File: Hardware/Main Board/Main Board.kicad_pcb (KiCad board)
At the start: 2 copper layers, 55 parts, among them J1 Micro_SD_Card_Det1, J2 Camera Module, J3 Conn_01x09_Socket, J4 MIC 1 Connector, J5 MIC 2 Connector, J6 USB_C_Receptacle_USB2.0_16P, J7 Conn_01x04_Socket, SW1 SW_Push, SW2 SW_Push, SW3 SW_Push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

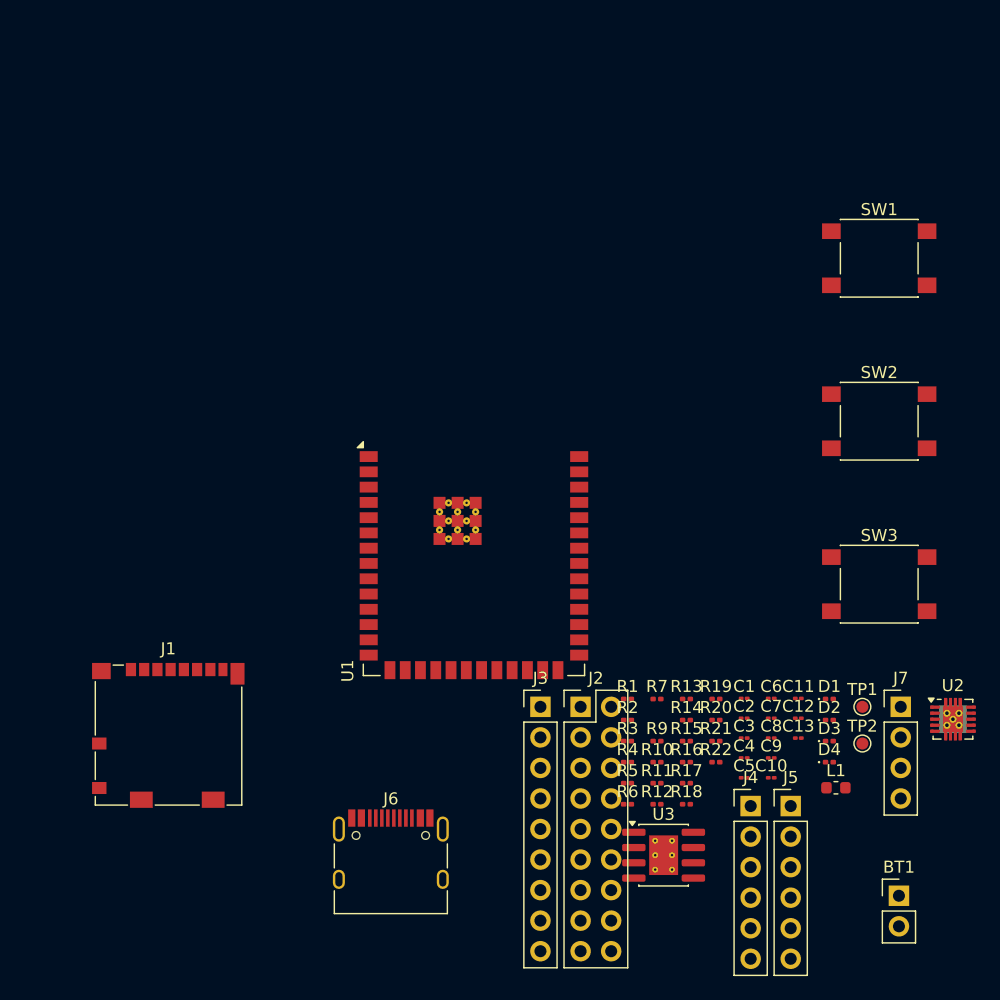
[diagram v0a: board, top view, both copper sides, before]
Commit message: drafted main board layout
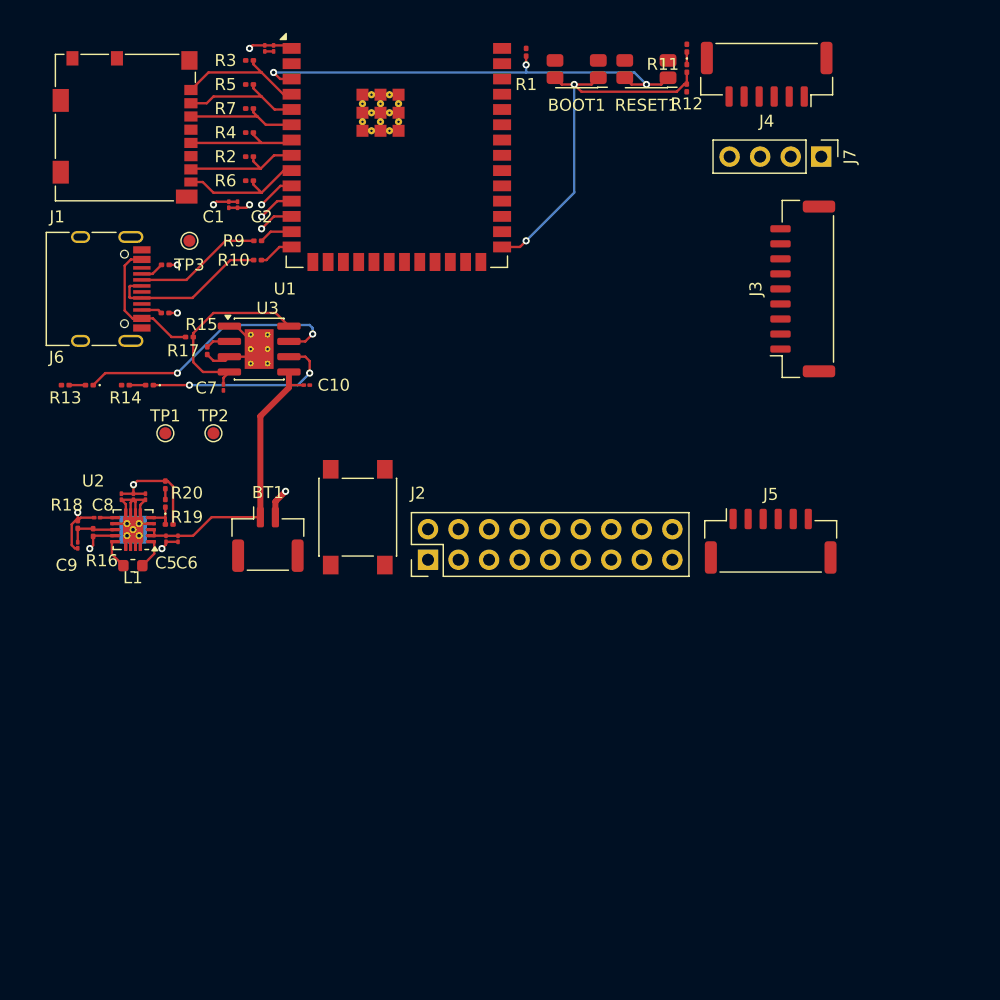
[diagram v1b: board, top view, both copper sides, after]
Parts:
- removed SW1, SW2, SW3: SW_Push, Button_Switch_SMD:SW_SPST_PTS645
- added BOOT1: SW_Push, Button_Switch_SMD:SW_SPST_EVQP7A, F.Cu at (119.2, 51.7)
- added RESET1: SW_Push, Button_Switch_SMD:SW_SPST_EVQP7A, F.Cu at (125.0, 51.7)
- added TP3: TestPoint, TestPoint:TestPoint_Pad_D1.0mm, F.Cu at (87.0, 66.0)
- added USER_INPUT1: SW_Push, Button_Switch_SMD:SW_SPST_PTS645, F.Cu at (101.0, 89.0)
- BT1: footprint Connector_PinHeader_2.54mm:PinHeader_1x02_P2.54mm_Vertical -> Connector_JST:JST_GH_SM02B-GHS-TB_1x02-1MP_P1.25mm_Horizontal
- J3: footprint Connector_PinHeader_2.54mm:PinHeader_1x09_P2.54mm_Vertical -> Connector_JST:JST_GH_SM09B-GHS-TB_1x09-1MP_P1.25mm_Horizontal
- J4, J5: footprint Connector_PinHeader_2.54mm:PinHeader_1x06_P2.54mm_Vertical -> Connector_JST:JST_GH_SM06B-GHS-TB_1x06-1MP_P1.25mm_Horizontal
- J7: value Conn_01x04_Socket -> OLED
- moved C4 70.8 mm to (94.0, 50.0), turned to 90 degrees
- moved U2 70.0 mm to (82.3, 90.0), turned to 180 degrees
- moved C3 69.8 mm to (93.3, 50.0), turned to -90 degrees
- moved D2 67.5 mm to (78.7, 78.0), turned to 180 degrees
- moved R5 66.1 mm to (92.0, 53.0), turned to 180 degrees
- moved R3 64.7 mm to (92.0, 51.0), turned to 180 degrees
- moved D3 63.8 mm to (83.7, 78.0), turned to 180 degrees
- moved TP1 62.3 mm to (85.0, 82.0)
- moved R22 61.7 mm to (85.0, 68.0)
- moved L1 61.3 mm to (82.3, 93.0)
- moved R4 61.1 mm to (92.0, 57.0)
- moved J4 60.9 mm to (135.0, 52.1), turned to 180 degrees
- moved R6 60.6 mm to (92.0, 61.0)
- moved C9 60.3 mm to (77.7, 91.3), turned to 90 degrees
- moved BT1 60.3 mm to (93.5, 90.8)
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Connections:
- J3 pad 7: I2C_SDA -> I2C_SCL
- J3 pad 8: I2C_SCL -> I2C_SDA
- J4 pad 2: MIC_LCRL -> GND
- J4 pad 3: MIC_DOUT -> MIC_BCLK
- J4 pad 4: MIC_BCLK -> MIC_DOUT
- J4 pad 5: MIC_GND -> MIC_LCRL
- J4 pad 6: MIC_3V -> +3.3V
- J5 pad 1: GND -> +3.3V
- J5 pad 2: MIC_LCRL -> GND
- J5 pad 3: MIC_DOUT -> MIC_BCLK
- J5 pad 4: MIC_BCLK -> MIC_DOUT
- J5 pad 5: MIC_GND -> MIC_LCRL
- J5 pad 6: MIC_3V -> GND
- U1 pad 10: CAM_D7 -> CAM_CLK
- U1 pad 11: CAM_PCLK -> CAM_SIO_DAT
- U1 pad 12: CAM_D0 -> CAM_HREF
- U1 pad 15: CAM_XCLK -> CAM_VSYNC
- U1 pad 16: CAM_HREF -> CAM_XCLK
- U1 pad 17: CAM_D1 -> CAM_PCLK
- U1 pad 18: CAM_D2 -> CAM_D6
- U1 pad 19: CAM_D3 -> CAM_D7
- U1 pad 22: CAM_D6 -> CAM_D2
- U1 pad 23: CAM_VSYNC -> CAM_D3
- U1 pad 24: CAM_SIO_DAT -> CAM_D0
- U1 pad 25: CAM_CLK -> CAM_D1
- U1 pad 26: CONTACT_MCLK -> Net-(U1-IO45)
- U1 pad 32: MIC_LCRL -> MIC_DOUT
- U1 pad 33: MIC_DOUT -> MIC_LCRL
- U1 pad 34: I2C_SDA -> CONTACT_SCLK
- U1 pad 35: I2C_SCL -> CONTACT_LRCK
- U1 pad 37: CONTACT_SCLK -> CONTACT_MCLK
- U1 pad 38: CONTACT_LRCK -> I2C_SCL
- U1 pad 39: Net-(U1-IO1) -> I2C_SDA
- U1 pad 4: SD_CLK -> SD_D2
- U1 pad 5: SD_CMD -> SD_D3
- U1 pad 6: SD_D0 -> SD_CMD
- U1 pad 7: SD_D1 -> SD_CLK
- U1 pad 8: SD_D2 -> SD_D0
- U1 pad 9: SD_D3 -> SD_D1
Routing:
- net Net-(U1-EN): track 0.00 -> 38.6 mm, vias 0 -> 3
- net GND: track 0.00 -> 34.2 mm, vias 0 -> 7
- net Net-(U1-IO0): track 0.00 -> 31.8 mm, vias 0 -> 2
- net +BATT: track 0.00 -> 24.3 mm
- net Net-(D2-K): track 0.00 -> 23.2 mm, vias 0 -> 2
- net Net-(D3-K): track 0.00 -> 16.3 mm, vias 0 -> 2
- net Net-(U3-CE): track 0.00 -> 16.1 mm
- net +3.3V: track 0.00 -> 15.1 mm, vias 0 -> 3
- net USB_D+: track 0.00 -> 13.6 mm
- net +5V_USB: track 0.00 -> 11.5 mm
- net SD_D2: track 0.00 -> 11.0 mm
- net SD_D1: track 0.00 -> 10.8 mm
- net USB_D-: track 0.00 -> 10.7 mm
- net SD_D3: track 0.00 -> 10.3 mm
- net SD_D0: track 0.00 -> 10.1 mm
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
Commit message: revised main board layout, rearranged around strapping pins, rererouted for noise
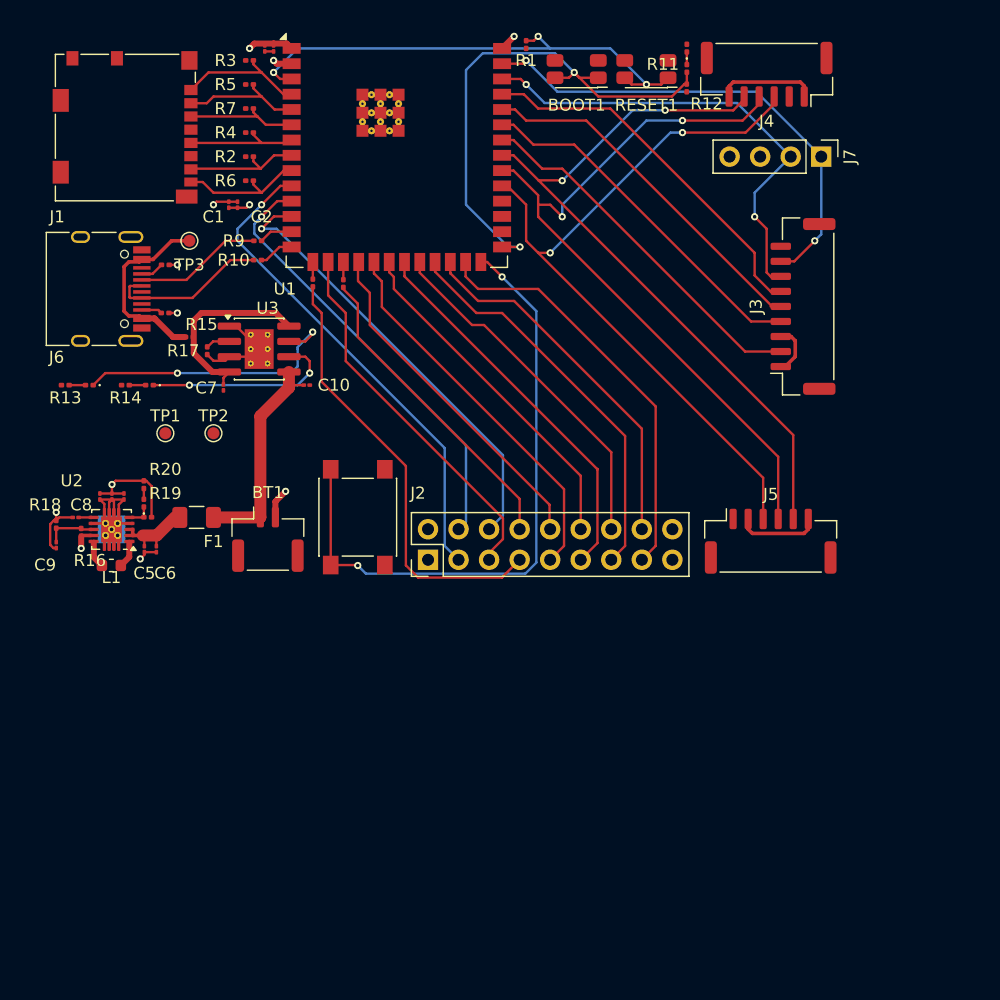
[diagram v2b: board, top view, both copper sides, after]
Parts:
- added F1: Fuse, Fuse:Fuse_1206_3216Metric, F.Cu at (87.6, 89.0)
- added R23: 22, Resistor_SMD:R_0201_0603Metric, F.Cu at (99.8, 69.6)
- added R8: 22, Resistor_SMD:R_0201_0603Metric, F.Cu at (97.3, 69.5)
- R16: value 1M -> 560k
- R18: value 111k -> 100k
- moved C5 1.99 mm to (83.3, 91.6)
- moved C6 1.99 mm to (84.3, 91.6)
- moved R19 1.89 mm to (83.5, 89.0)
- moved C8 1.79 mm to (77.5, 89.0)
- moved C9 1.79 mm to (75.9, 91.3)
- moved L1 1.79 mm to (80.5, 93.0)
- moved R18 1.79 mm to (75.9, 89.6)
- moved R20 1.79 mm to (83.2, 86.3)
- moved C11 1.79 mm to (79.6, 87.3)
- moved C12 1.79 mm to (81.6, 87.3)
- moved C13 1.79 mm to (80.6, 87.3)
- moved D4 1.79 mm to (83.2, 87.8)
- moved U2 1.79 mm to (80.5, 90.0)
- moved J3 1.46 mm to (138.0, 71.5)
- moved R16 0.99 mm to (78.0, 90.2)
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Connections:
- C5 pad 2: +BATT -> Net-(U2-EN)
- C6 pad 2: +BATT -> Net-(U2-EN)
- U1 pad 15: CAM_VSYNC -> Net-(U1-IO3)
- U1 pad 16: CAM_XCLK -> CAM_VSYNC
- U1 pad 17: CAM_PCLK -> Net-(U1-IO9)
- U2 pad 2: +BATT -> Net-(U2-EN)
- U2 pad 3: +BATT -> Net-(U2-EN)
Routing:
- net MIC_DOUT: track 0.00 -> 62.9 mm, vias 0 -> 2
- net MIC_BCLK: track 0.00 -> 62.3 mm, vias 0 -> 2
- net MIC_LCRL: track 0.00 -> 61.0 mm, vias 0 -> 2
- net Net-(U1-IO45): track 0.00 -> 52.9 mm, vias 0 -> 2
- net I2C_SDA: track 0.00 -> 41.4 mm, vias 0 -> 2
- net I2C_SCL: track 0.00 -> 39.8 mm, vias 0 -> 2
- net CAM_CLK: track 3.15 -> 41.1 mm
- net CAM_PCLK: track 0.00 -> 36.9 mm
- net CAM_D1: track 0.00 -> 34.7 mm
- net CAM_HREF: track 2.93 -> 37.4 mm
- net CAM_SIO_DAT: track 3.04 -> 36.8 mm
- net CAM_D3: track 0.00 -> 33.0 mm
- net CAM_D5: track 0.00 -> 32.0 mm
- net CAM_D7: track 0.00 -> 31.8 mm
- net CAM_VSYNC: track 0.00 -> 31.3 mm
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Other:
- board text added: "${REFERENCE}"

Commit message: reviewed most of main board, getting ready to finalize and prepare for manufacturing
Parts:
- added D5: SS14, Diode_SMD:D_SMA, F.Cu at (81.0, 80.0)
- added H1: MountingHole, MountingHole:MountingHole_2.1mm, F.Cu at (96.0, 82.0)
- added H2: MountingHole, MountingHole:MountingHole_2.1mm, F.Cu at (140.0, 84.0)
- added Q1: AO3401A, Package_TO_SOT_SMD:SOT-23, F.Cu at (91.1, 82.0)
- added R24: 100k, Resistor_SMD:R_0402_1005Metric, F.Cu at (76.0, 81.0)
- added TP4: TestPoint, TestPoint:TestPoint_Pad_1.0x1.0mm, F.Cu at (91.0, 87.5)
- added TP5: TestPoint, TestPoint:TestPoint_Pad_1.0x1.0mm, F.Cu at (95.5, 86.0)
- C1, C10, C2, C3, C7, C8, C9: footprint Capacitor_SMD:C_01005_0402Metric -> Capacitor_SMD:C_0402_1005Metric
- C11, C12, C13: footprint Capacitor_SMD:C_01005_0402Metric -> Capacitor_SMD:C_0805_2012Metric
- C4, C5, C6: footprint Capacitor_SMD:C_01005_0402Metric -> Capacitor_SMD:C_0603_1608Metric
- D1, D2, D3, D4: footprint LED_SMD:LED_0201_0603Metric -> LED_SMD:LED_0603_1608Metric
- L1: footprint Inductor_SMD:L_0603_1608Metric -> Inductor_SMD:L_Bourns-SRN4018
- R1, R10, R11, R12, R13, R14, R15, R16, R17, R18, R19, R2, R20, R21, R22, R23, R3, R4, R5, R6, R7, R8, R9: footprint Resistor_SMD:R_0201_0603Metric -> Resistor_SMD:R_0402_1005Metric
- TP1, TP2, TP3: footprint TestPoint:TestPoint_Pad_D1.0mm -> Connector_PinHeader_2.54mm:PinHeader_1x01_P2.54mm_Vertical
- moved R12 19.9 mm to (115.0, 68.0)
- moved D1 13.2 mm to (139.9, 56.4), turned to 180 degrees
- moved R11 12.2 mm to (140.1, 54.9), turned to 0 degrees
- moved TP1 11.0 mm to (88.0, 92.6)
- moved TP2 7.07 mm to (88.0, 89.0)
- moved C12 4.37 mm to (78.5, 84.1)
- moved C11 4.34 mm to (82.5, 84.1)
- moved F1 4.24 mm to (89.0, 85.0)
- moved R20 3.90 mm to (84.6, 82.6), turned to 180 degrees
- moved D4 3.35 mm to (84.4, 84.7)
- moved C13 3.16 mm to (80.5, 84.1)
- moved R18 3.07 mm to (76.0, 86.5)
- moved C6 2.89 mm to (85.5, 89.0)
- moved C9 2.82 mm to (76.0, 88.5)
- moved C5 2.72 mm to (84.0, 89.0)
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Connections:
- F1 pad 1: +BATT -> VIN
- R8 pad 1: Net-(U1-IO3) -> Net-(U1-IO46)
- U1 pad 15: Net-(U1-IO3) -> CAM_VSYNC
- U1 pad 16: CAM_VSYNC -> Net-(U1-IO46)
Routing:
- net GND: track 47.0 -> 124.0 mm, vias 8 -> 16
- net +3.3V: track 23.4 -> 59.0 mm, vias 4 -> 18
- net +5V_USB: track 16.1 -> 49.3 mm
- net VIN: track 0.00 -> 13.3 mm
- net CAM_PCLK: track 36.9 -> 28.6 mm
- net Net-(U1-IO0): track 44.4 -> 49.9 mm
- net USB_D-: track 10.7 -> 12.7 mm
- net Net-(U2-EN): track 6.51 -> 8.38 mm
- net Net-(U1-IO46): track 0.00 -> 1.83 mm
- net Net-(D2-K): track 23.4 -> 21.9 mm
- net Net-(U1-IO3): track 1.43 -> 0.00 mm
- net Net-(U1-EN): track 41.4 -> 42.8 mm
- net Net-(D4-K): track 1.83 -> 3.19 mm
- net Net-(U2-L2): track 2.18 -> 3.25 mm
- net Net-(U2-L1): track 2.20 -> 3.23 mm
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- added copper zone on In2.Cu, net +3.3V
- added copper zone on In1.Cu, net GND
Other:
- board outline added: 70 x 48 mm
- copper layers 2 -> 4
- board text removed: "${REFERENCE}"

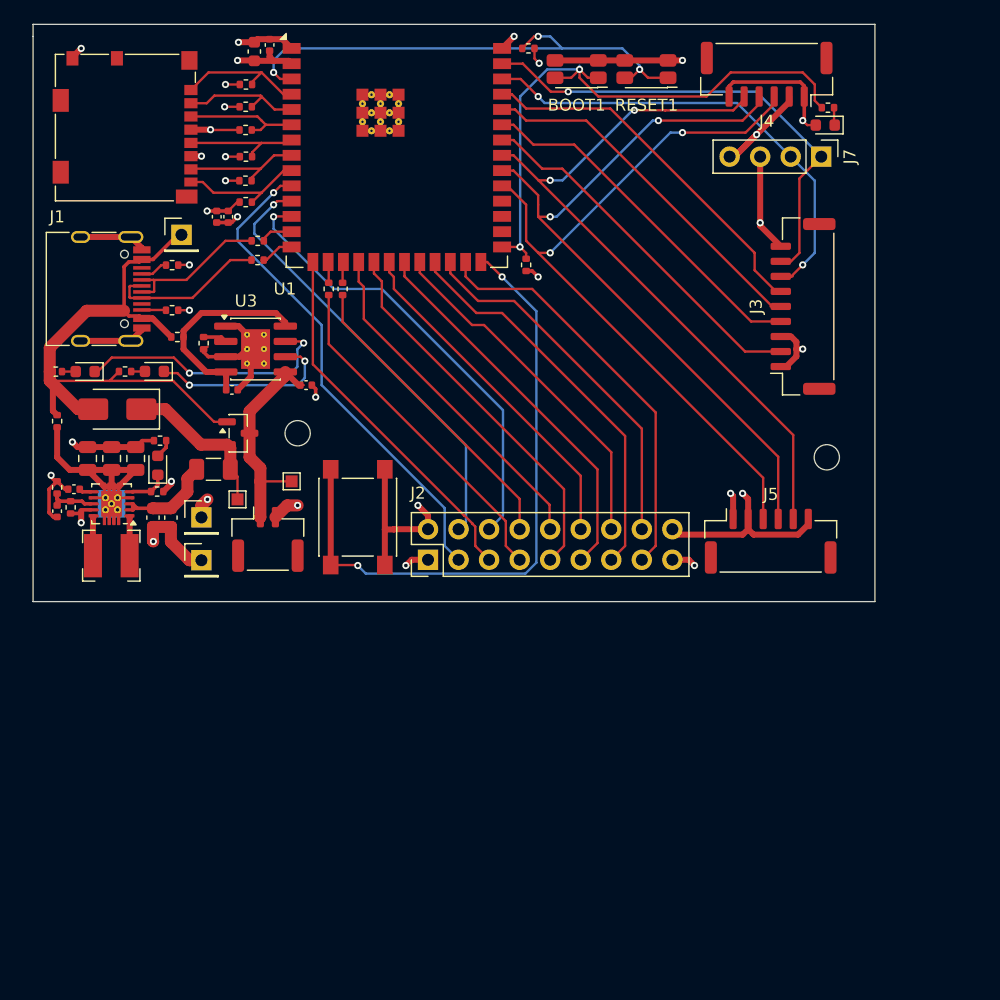
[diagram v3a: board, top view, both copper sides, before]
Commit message: fixed sd card, checked manufacturing feasibility and cleaned up board layout
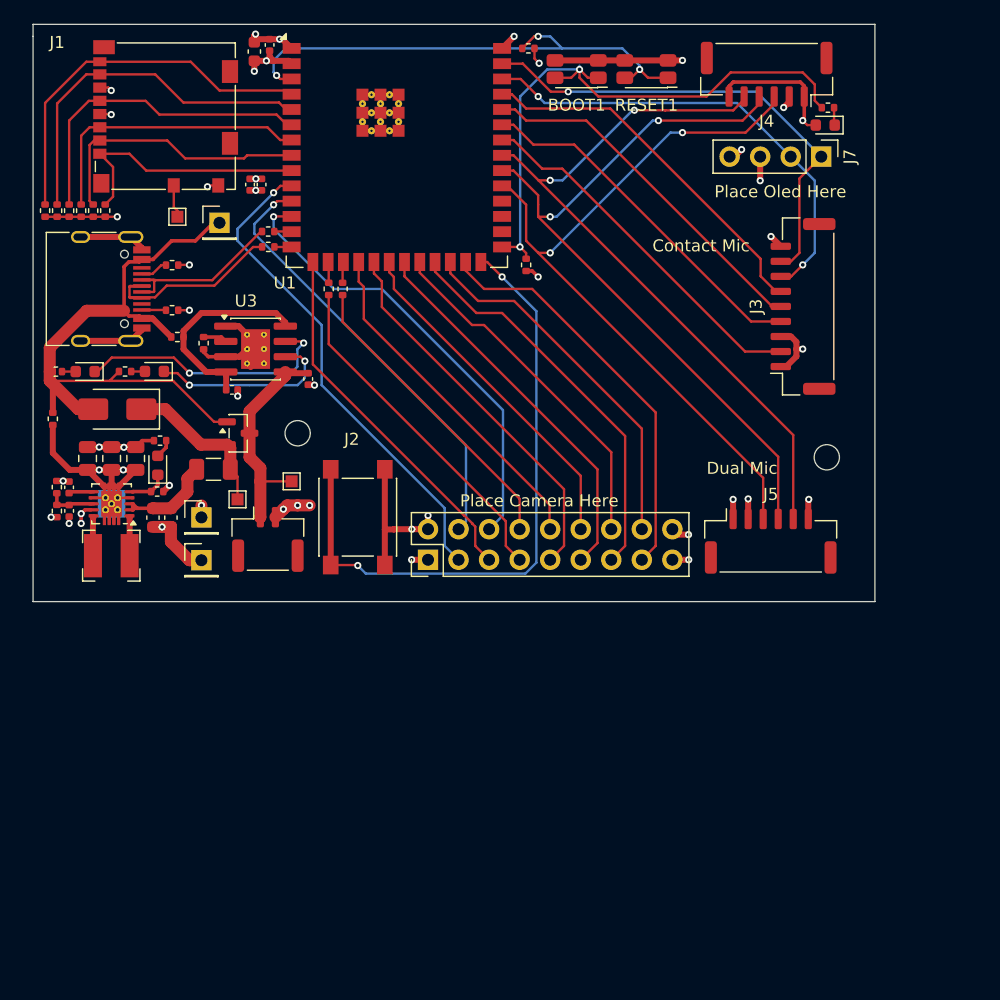
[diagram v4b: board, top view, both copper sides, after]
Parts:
- added TP6: TestPoint, TestPoint:TestPoint_Pad_1.0x1.0mm, F.Cu at (86.0, 64.0)
- moved R6 16.7 mm to (75.0, 63.5), turned to 90 degrees
- moved R2 15.9 mm to (76.0, 63.5), turned to 90 degrees
- moved R3 15.7 mm to (80.0, 63.5), turned to -90 degrees
- moved R4 15.4 mm to (77.0, 63.5), turned to 90 degrees
- moved R5 15.3 mm to (79.0, 63.5), turned to -90 degrees
- moved R7 15.2 mm to (78.0, 63.5), turned to -90 degrees
- moved C1 3.85 mm to (92.0, 61.3)
- moved C2 3.85 mm to (93.0, 61.3)
- moved J1 3.45 mm to (85.0, 55.7), turned to 90 degrees
- moved TP3 3.32 mm to (89.5, 64.5)
- moved R10 1.41 mm to (93.6, 66.5)
- moved R16 1.18 mm to (76.0, 88.5)
- moved R9 1.16 mm to (93.5, 65.2)
- moved C9 1.00 mm to (77.0, 88.5)
- moved C10 0.54 mm to (96.9, 77.5), turned to 90 degrees
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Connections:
- net USB_D+ renamed /D+
- net USB_D- renamed /D-
- J1 pad 9: unconnected-(J1-DET-Pad9) -> Net-(J1-DET)
- U1 pad 4: SD_D2 -> SD_D1
- U1 pad 5: SD_D3 -> SD_D0
- U1 pad 6: SD_CMD -> SD_CLK
- U1 pad 7: SD_CLK -> SD_CMD
- U1 pad 8: SD_D0 -> SD_D3
- U1 pad 9: SD_D1 -> SD_D2
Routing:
- net GND: track 124.0 -> 95.3 mm, vias 16 -> 27
- net SD_D1: track 10.6 -> 31.5 mm
- net SD_D0: track 10.2 -> 30.1 mm
- net SD_CLK: track 9.94 -> 27.0 mm
- net +3.3V: track 59.0 -> 43.3 mm, vias 18 -> 20
- net SD_CMD: track 10.0 -> 24.5 mm
- net SD_D3: track 10.3 -> 22.7 mm
- net SD_D2: track 11.1 -> 21.8 mm
- net /D+: track 13.6 -> 18.1 mm
- net +5V_USB: track 49.3 -> 52.2 mm
- net Net-(J1-DET): track 0.00 -> 2.73 mm
- net /D-: track 12.7 -> 14.7 mm
- net Net-(U1-USB_D+/IO20): track 2.97 -> 1.44 mm
- net Net-(U1-USB_D-/IO19): track 2.81 -> 1.45 mm
- net Net-(U2-VAUX): track 0.98 -> 2.23 mm
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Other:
- board text added: "Contact Mic"
- board text added: "Dual Mic"
- board text added: "Place Camera Here"
- board text added: "Place Oled Here"
